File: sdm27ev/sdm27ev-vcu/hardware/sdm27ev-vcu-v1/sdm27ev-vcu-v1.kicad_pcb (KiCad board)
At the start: 2 copper layers, 100 x 60 mm, 6 parts, among them J1 6437288-1, J2 6437288-1, U1 ESP32-P4

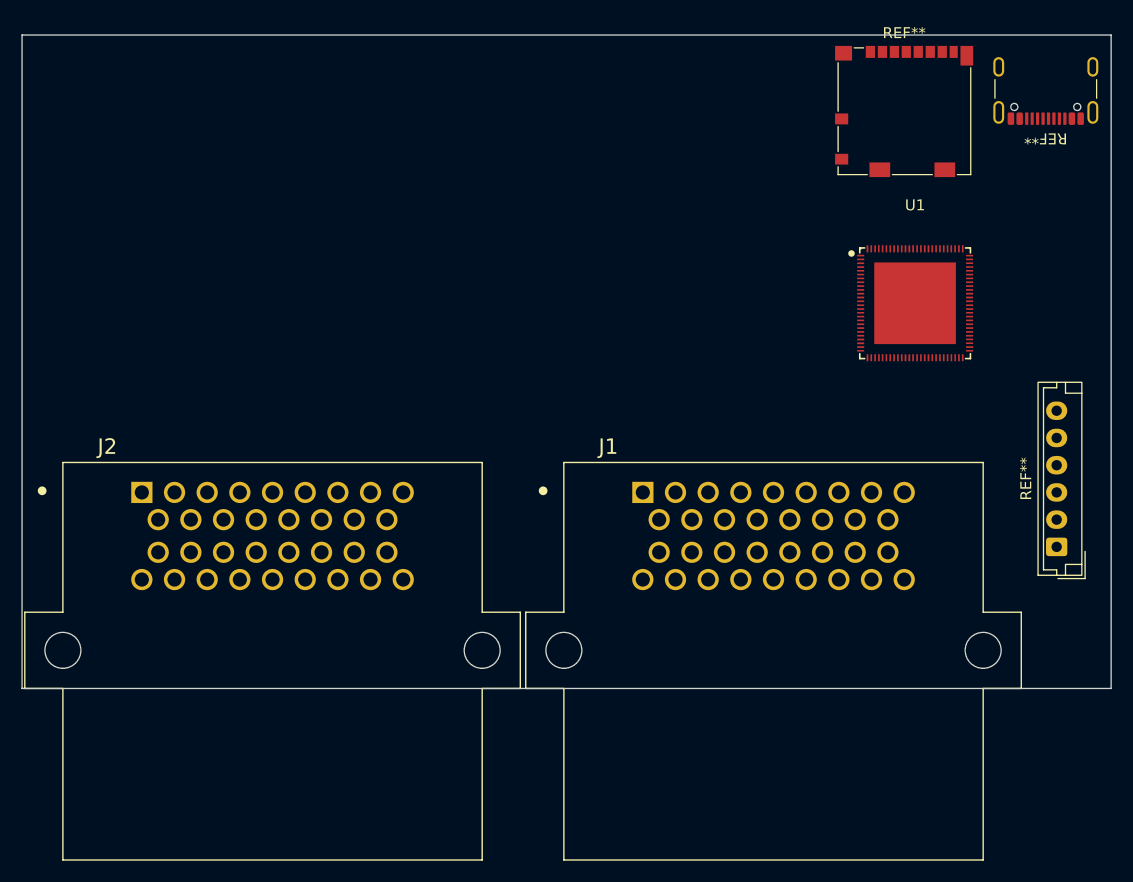
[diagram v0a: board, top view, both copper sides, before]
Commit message: added all hierarchical sheet pins, added can termination optocouplers
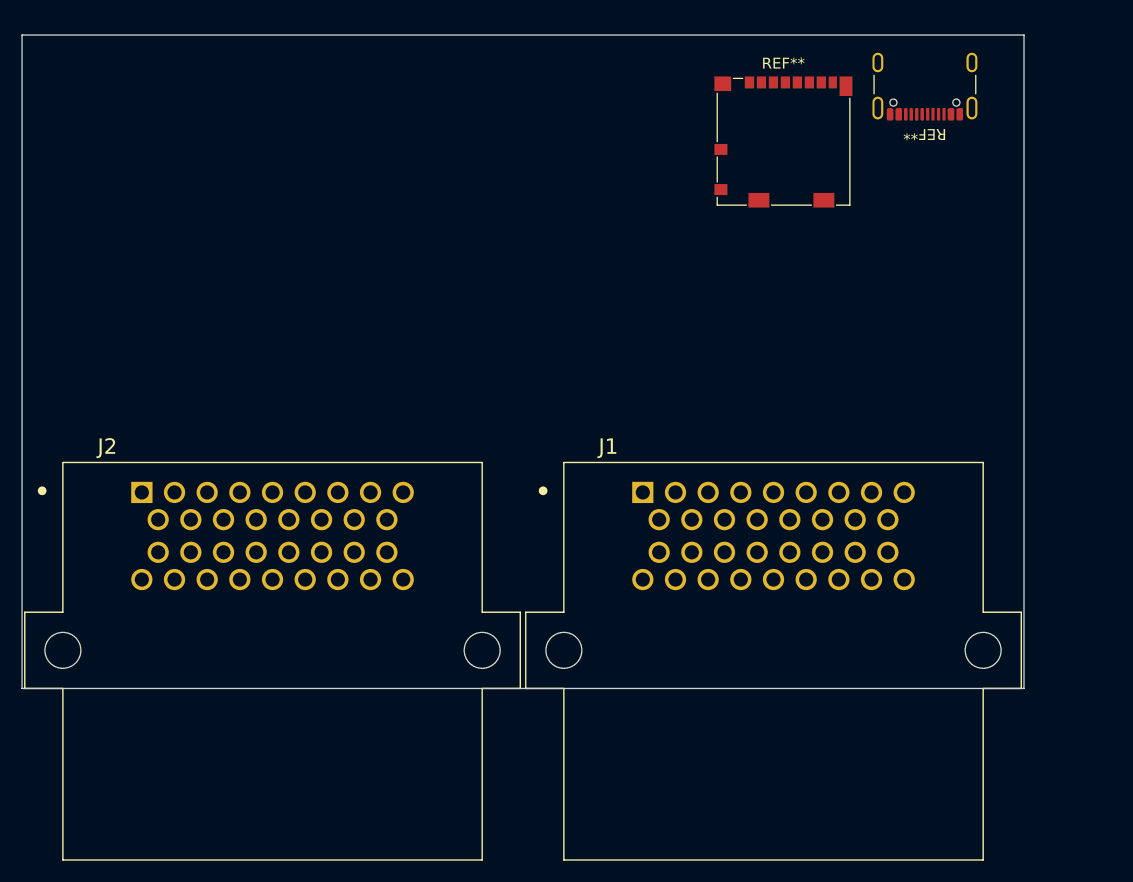
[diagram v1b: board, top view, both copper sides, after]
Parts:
- removed the REF** at (145.0, 118.0)
- removed U1: ESP32-P4, SDM27 EV VCU:QFN-104_L10.0-W10.0-P0.35-TL-EP7.5
- moved REF** 11.4 mm to (119.9, 80.8)
- moved REF** 11.1 mm to (132.9, 74.6)
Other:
- board size 100 x 60 mm -> 92 x 60 mm
